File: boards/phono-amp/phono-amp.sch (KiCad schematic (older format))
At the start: 27 parts, among them J1 Conn_Coaxial, J2 Conn_01x06_Male, J3 Conn_Coaxial, U1 6DJ8

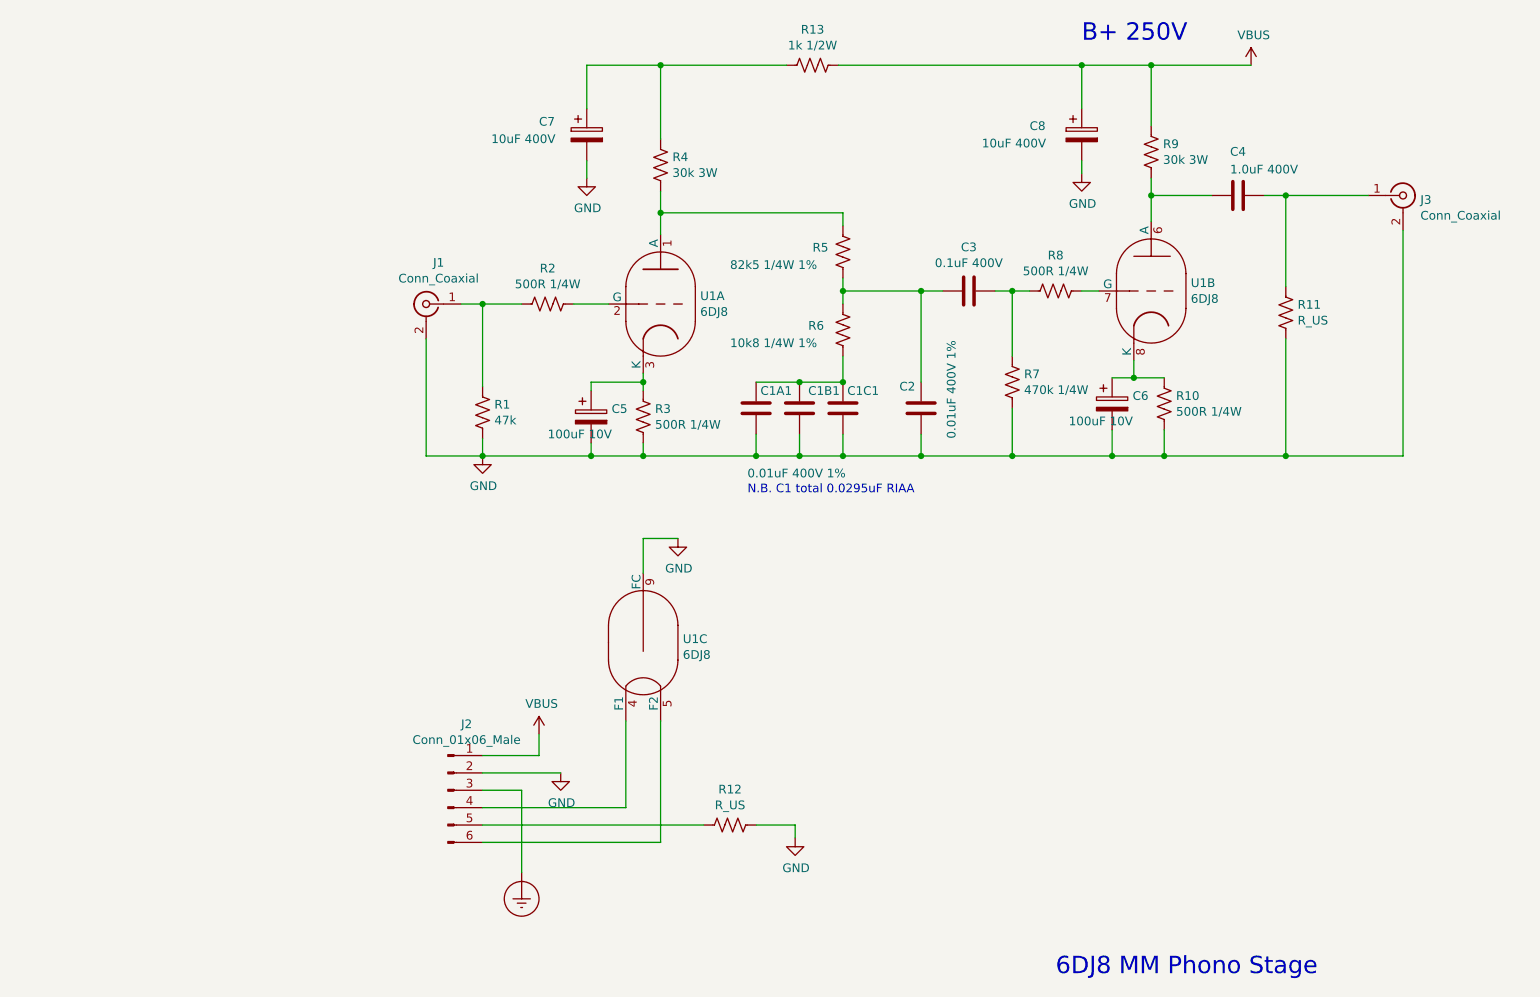
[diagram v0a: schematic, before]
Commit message: footprints done, starting placement
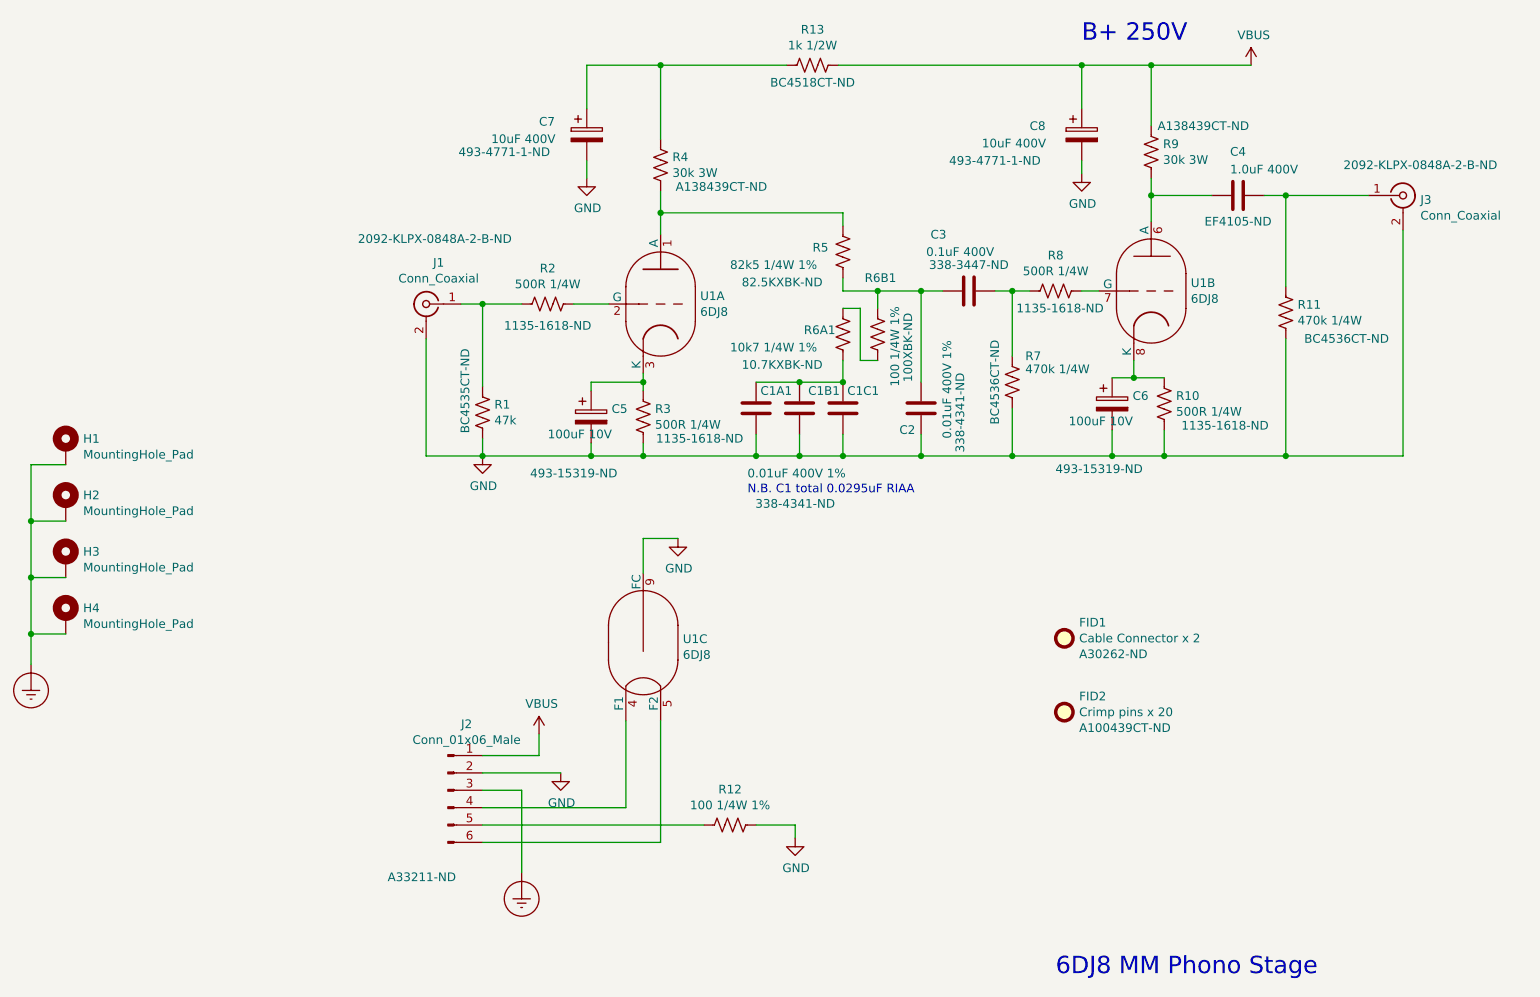
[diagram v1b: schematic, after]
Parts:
- added FID1: Cable Connector x 2, symbol Mechanical:Fiducial
- added FID2: Crimp pins x 20, symbol Mechanical:Fiducial
- added H1, H2, H3, H4: MountingHole_Pad, symbol Mechanical:MountingHole_Pad
- added R6B1: 100 1/4W 1%, Resistor_THT:R_Axial_DIN0207_L6.3mm_D2.5mm_P10.16mm_Horizontal, symbol Device:R_US
- C1A1, C1B1, C1C1, C2: footprint (none) -> my-capacitors:CAP_L20_W6.4_P9.5; CatNo (none) -> 338-4341-ND; Vendor (none) -> DigiKey
- C3: footprint (none) -> my-capacitors:CAP_L20_W13_P9.5; CatNo (none) -> 338-3447-ND; Vendor (none) -> DigiKey
- C4: footprint (none) -> my-capacitors:CAP_L26_W8.5_P22.5; CatNo (none) -> EF4105-ND; Vendor (none) -> DigiKey
- C5, C6: footprint (none) -> Capacitor_THT:CP_Radial_D5.0mm_P2.00mm; CatNo (none) -> 493-15319-ND; Vendor (none) -> DigiKey
- C7, C8: footprint (none) -> Capacitor_THT:CP_Radial_D10.0mm_P5.00mm; CatNo (none) -> 493-4771-1-ND; Vendor (none) -> DigiKey
- J1, J3: footprint (none) -> my-connectors:rca-single-klpx; CatNo (none) -> 2092-KLPX-0848A-2-B-ND; Vendor (none) -> DigiKey
- J2: footprint (none) -> Connector_Molex:Molex_Micro-Fit_3.0_43650-0615_1x06_P3.00mm_Vertical; CatNo (none) -> A33211-ND; Vendor (none) -> DigiKey
- R1: footprint (none) -> Resistor_THT:R_Axial_DIN0414_L11.9mm_D4.5mm_P15.24mm_Horizontal; CatNo (none) -> BC4535CT-ND; Vendor (none) -> DigiKey
- R10, R2, R3, R8: footprint (none) -> Resistor_THT:R_Axial_DIN0411_L9.9mm_D3.6mm_P15.24mm_Horizontal; CatNo (none) -> 1135-1618-ND; Vendor (none) -> DigiKey
- R11: value R_US -> 470k 1/4W; footprint (none) -> Resistor_THT:R_Axial_DIN0207_L6.3mm_D2.5mm_P10.16mm_Horizontal; CatNo (none) -> BC4536CT-ND; Vendor (none) -> DigiKey
- R12: value R_US -> 100 1/4W 1%; footprint (none) -> Resistor_THT:R_Axial_DIN0207_L6.3mm_D2.5mm_P10.16mm_Horizontal; CatNo (none) -> 100XBK-ND; Vendor (none) -> DigiKey
- R13: footprint (none) -> Resistor_THT:R_Axial_DIN0414_L11.9mm_D4.5mm_P15.24mm_Horizontal; CatNo (none) -> BC4518CT-ND; Vendor (none) -> DigiKey
- R4, R9: footprint (none) -> Resistor_THT:R_Axial_DIN0516_L15.5mm_D5.0mm_P20.32mm_Horizontal; CatNo (none) -> A138439CT-ND; Vendor (none) -> DigiKey
- R5: footprint (none) -> Resistor_THT:R_Axial_DIN0207_L6.3mm_D2.5mm_P10.16mm_Horizontal; CatNo (none) -> 82.5KXBK-ND; Vendor (none) -> DigiKey
- R6A1: renamed from R6; value 10k8 1/4W 1% -> 10k7 1/4W 1%; footprint (none) -> Resistor_THT:R_Axial_DIN0207_L6.3mm_D2.5mm_P10.16mm_Horizontal; CatNo (none) -> 10.7KXBK-ND; Vendor (none) -> DigiKey
- R7: footprint (none) -> Resistor_THT:R_Axial_DIN0207_L6.3mm_D2.5mm_P10.16mm_Horizontal; CatNo (none) -> BC4536CT-ND; Vendor (none) -> DigiKey
- U1: footprint Valve:Valve_Noval_P -> my-capacitors:P-ST9-700-PC; CatNo (none) -> P-STD-700-PC & P-SS9-400; Vendor (none) -> AES
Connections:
- net Earth_Protective: now also H1.1, H2.1, H3.1, H4.1
- net at C2.1, C3.2, R5.1: now also R6B1.2; no longer R6A1.2
- new net: R6A1.2, R6B1.1
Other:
- moved on the sheet: R6A1

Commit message: Amp PCB done?
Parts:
- added H5: MountingHole_Pad, MountingHole:MountingHole_4.3mm_M4_ISO7380_Pad, symbol Mechanical:MountingHole_Pad
- added JP1: Jumper_NC_Dual, Connector_PinHeader_2.54mm:PinHeader_1x03_P2.54mm_Vertical, symbol Device:Jumper_NC_Dual
- H1, H2, H3, H4: footprint (none) -> MountingHole:MountingHole_4.3mm_M4_ISO7380_Pad
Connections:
- net Earth_Protective: now also JP1.1
- net GND: now also H5.1, JP1.3
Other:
- note added: "Chassis\nGND"
- note added: "Turntable\nGND"
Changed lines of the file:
@@
 F 0 "H4" H 1500 4749 50  0000 L CNN
 F 1 "MountingHole_Pad" H 1500 4658 50  0000 L CNN
-F 2 "" H 1400 4700 50  0001 C CNN
+F 2 "MountingHole:MountingHole_4.3mm_M4_ISO7380_Pad" H 1400 4700 50  0001 C CNN
 F 3 "~" H 1400 4700 50  0001 C CNN
 	1    1400 4700
@@
 F 0 "H3" H 1500 4424 50  0000 L CNN
 F 1 "MountingHole_Pad" H 1500 4333 50  0000 L CNN
-F 2 "" H 1400 4375 50  0001 C CNN
+F 2 "MountingHole:MountingHole_4.3mm_M4_ISO7380_Pad" H 1400 4375 50  0001 C CNN
 F 3 "~" H 1400 4375 50  0001 C CNN
 	1    1400 4375
@@
 F 0 "H2" H 1500 4099 50  0000 L CNN
 F 1 "MountingHole_Pad" H 1500 4008 50  0000 L CNN
-F 2 "" H 1400 4050 50  0001 C CNN
+F 2 "MountingHole:MountingHole_4.3mm_M4_ISO7380_Pad" H 1400 4050 50  0001 C CNN
 F 3 "~" H 1400 4050 50  0001 C CNN
 	1    1400 4050
@@
 F 0 "H1" H 1500 3774 50  0000 L CNN
 F 1 "MountingHole_Pad" H 1500 3683 50  0000 L CNN
-F 2 "" H 1400 3725 50  0001 C CNN
+F 2 "MountingHole:MountingHole_4.3mm_M4_ISO7380_Pad" H 1400 3725 50  0001 C CNN
 F 3 "~" H 1400 3725 50  0001 C CNN
 	1    1400 3725
@@
 	1    0    0    -1
 $EndComp
+$Comp
+L Mechanical:MountingHole_Pad H5
+U 1 1 608ED4CC
+P 1400 2900
+F 0 "H5" H 1500 2949 50  0000 L CNN
+F 1 "MountingHole_Pad" H 1500 2858 50  0000 L CNN
+F 2 "MountingHole:MountingHole_4.3mm_M4_ISO7380_Pad" H 1400 2900 50  0001 C CNN
+F 3 "~" H 1400 2900 50  0001 C CNN
+	1    1400 2900
+	1    0    0    -1
+$EndComp
+$Comp
+L power:GND #PWR0101
+U 1 1 608ED922
+P 1400 3125
+F 0 "#PWR0101" H 1400 2875 50  0001 C CNN
+F 1 "GND" H 1405 2952 50  0000 C CNN
+F 2 "" H 1400 3125 50  0001 C CNN
+F 3 "" H 1400 3125 50  0001 C CNN
+	1    1400 3125
+	1    0    0    -1
+$EndComp
+Wire Wire Line
+	1400 3125 1400 3000
+Text Notes 1250 2550 0    100  ~ 0
+Turntable\nGND
+Text Notes 2375 4400 0    100  ~ 0
+Chassis\nGND
+$Comp
+L Device:Jumper_NC_Dual JP1
+U 1 1 608F7447
+P 4050 4400
+F 0 "JP1" H 4050 4639 50  0000 C CNN
+F 1 "Jumper_NC_Dual" H 4050 4548 50  0000 C CNN
+F 2 "Connector_PinHeader_2.54mm:PinHeader_1x03_P2.54mm_Vertical" H 4050 4400 50  0001 C CNN
+F 3 "~" H 4050 4400 50  0001 C CNN
+	1    4050 4400
+	1    0    0    -1
+$EndComp
+Wire Wire Line
+	4425 4850 4050 4850
+Wire Wire Line
+	4050 4850 4050 4500
+$Comp
+L power:GND #PWR012
+U 1 1 608FFA77
+P 4300 4400
+F 0 "#PWR012" H 4300 4150 50  0001 C CNN
+F 1 "GND" H 4305 4227 50  0000 C CNN
+F 2 "" H 4300 4400 50  0001 C CNN
+F 3 "" H 4300 4400 50  0001 C CNN
+	1    4300 4400
+	1    0    0    -1
+$EndComp
+$Comp
+L power:Earth_Protective #PWR011
+U 1 1 608FFFE0
+P 3800 4400
+F 0 "#PWR011" H 4050 4150 50  0001 C CNN
+F 1 "Earth_Protective" H 4250 4250 50  0001 C CNN
+F 2 "" H 3800 4300 50  0001 C CNN
+F 3 "~" H 3800 4300 50  0001 C CNN
+	1    3800 4400
+	1    0    0    -1
+$EndComp
